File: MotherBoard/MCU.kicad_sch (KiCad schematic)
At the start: 50 parts, among them J201 Conn_ARM_SWD_TagConnect_TC2030, J202 Micro_SD_Card_Det1, U201 STM32F205RBTx, Y201 16 Mhz

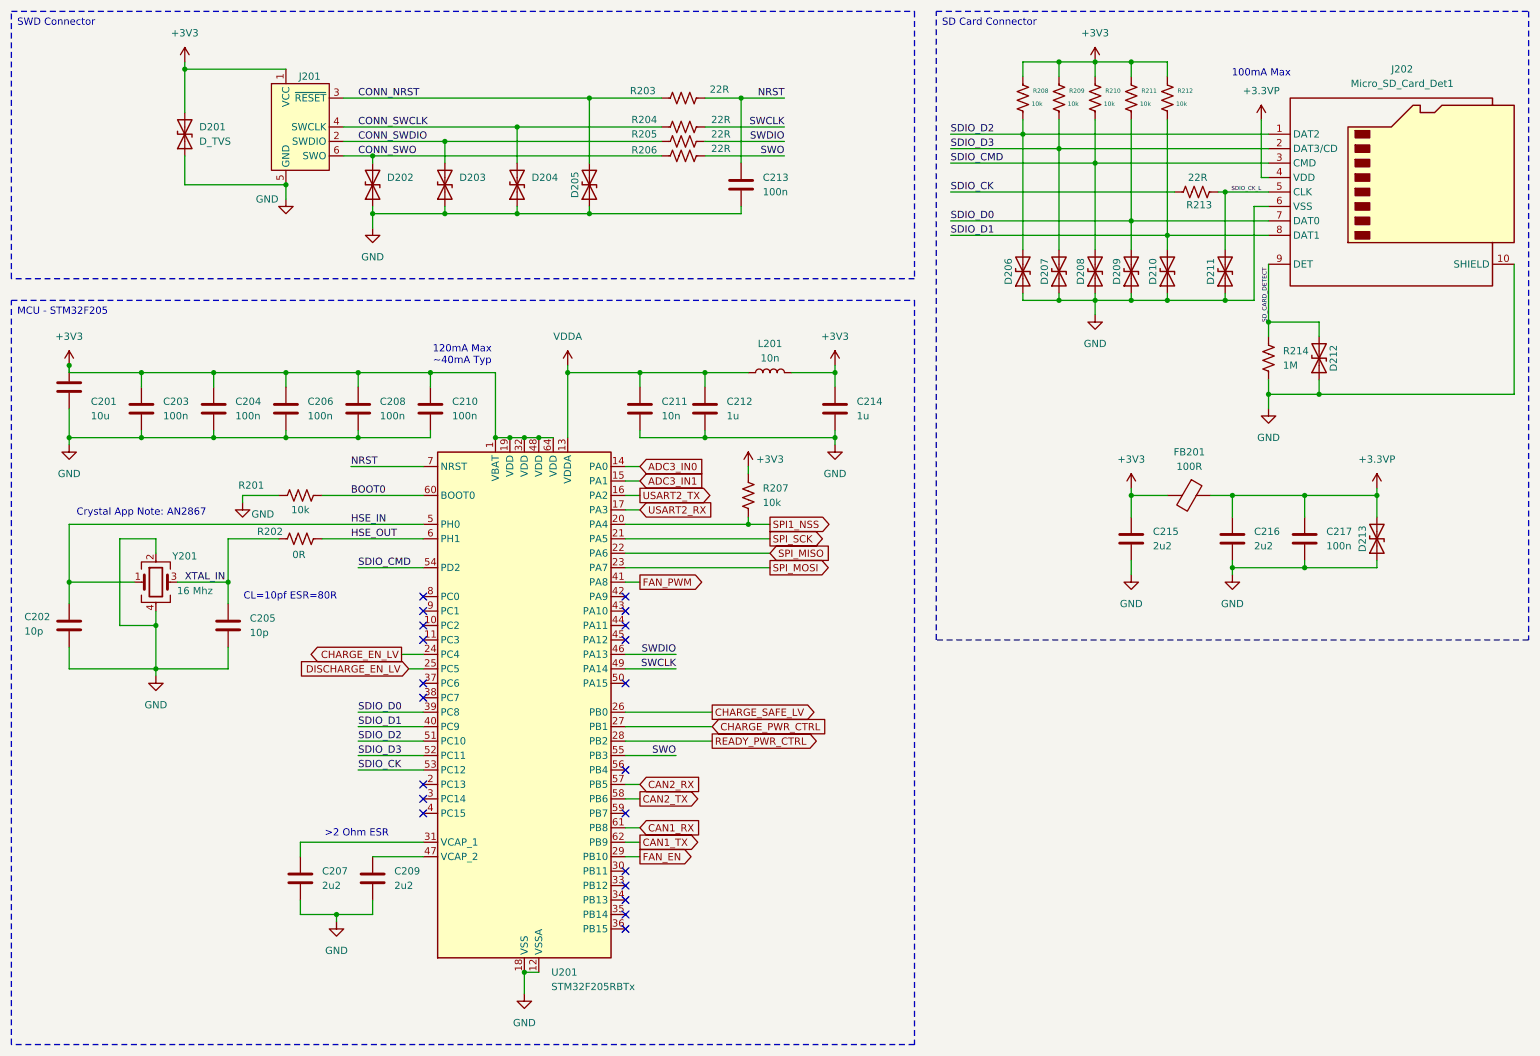
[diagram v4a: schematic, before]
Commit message: Fixed BQ79600 + minor changes
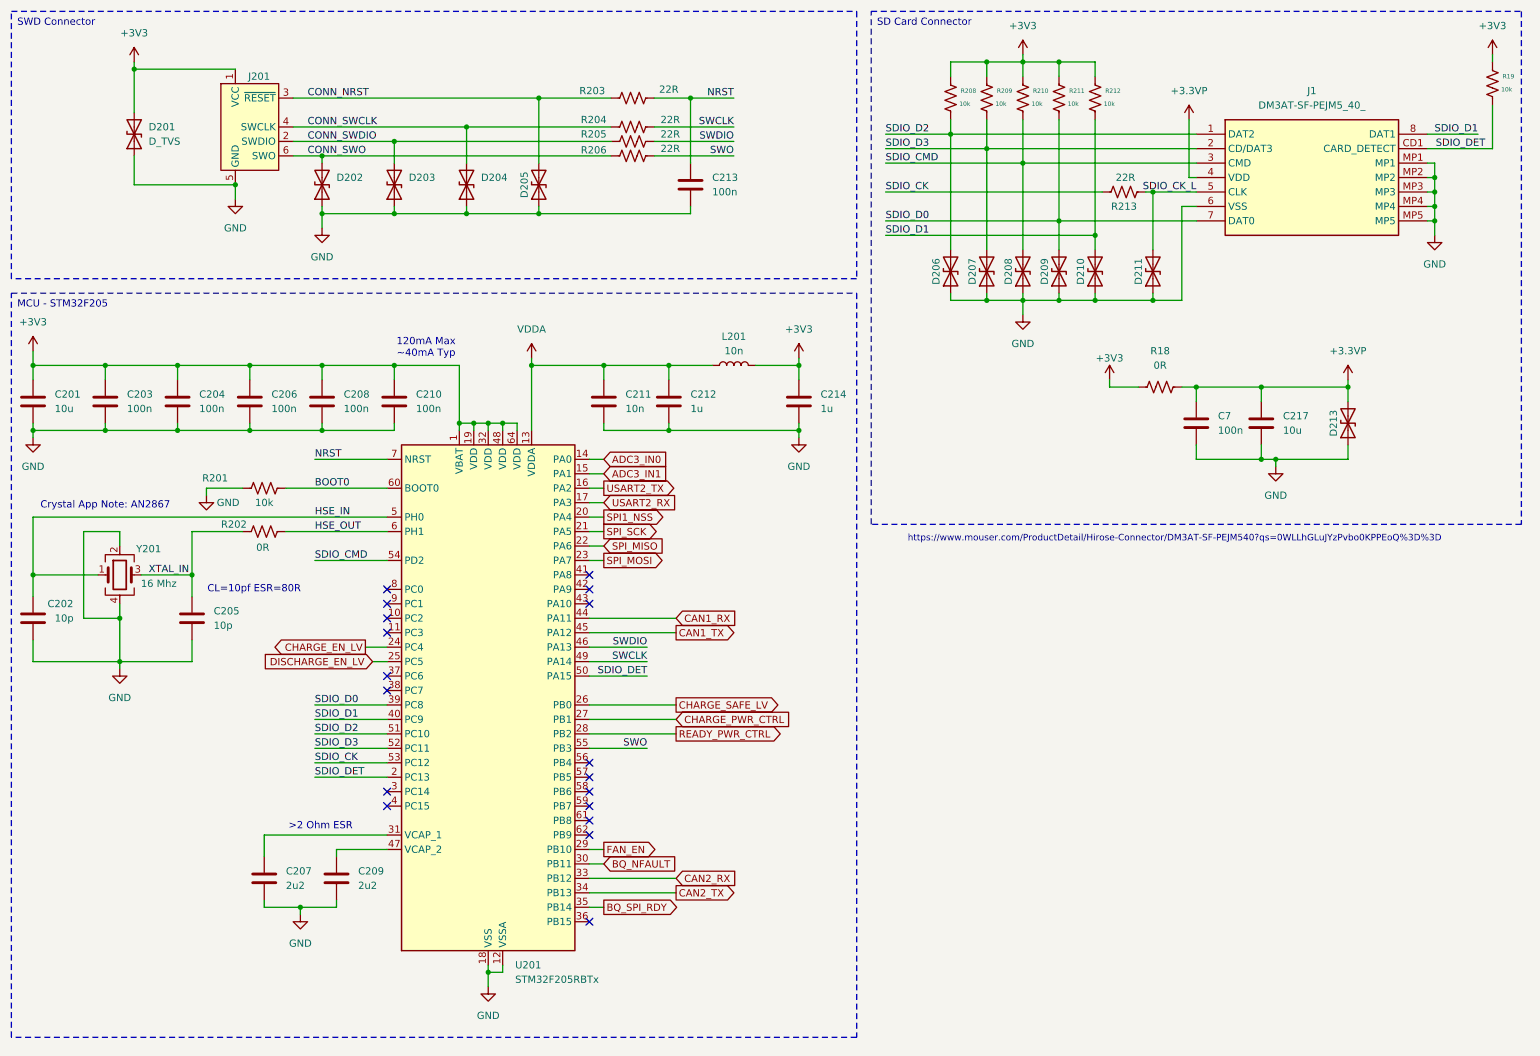
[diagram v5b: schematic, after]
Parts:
- removed C215, C216: 2u2, symbol Device:C
- removed D212: D_TVS, Diode_SMD:D_SOD-323, symbol Device:D_TVS
- removed FB201: 100R, symbol Device:FerriteBead
- removed J202: Micro_SD_Card_Det1, symbol Connector:Micro_SD_Card_Det1
- removed R207: 10k, Resistor_SMD:R_0402_1005Metric, symbol Device:R_US
- removed R214: 1M, Resistor_SMD:R_0402_1005Metric, symbol Device:R_US
- added C7: 100n, symbol Device:C
- added J1: DM3AT-SF-PEJM5_40_, SDIO:SD_CARD, symbol SDIO:DM3AT-SF-PEJM5_40_
- added R18: 0R, Resistor_SMD:R_0402_1005Metric, symbol Device:R_US
- added R19: 10k, Resistor_SMD:R_0402_1005Metric, symbol Device:R_US
- C217: value 100n -> 10u
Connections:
- net +3.3VP: now also C7.1, J1.4 (VDD), R18.2
- net +3V3: now also R18.1, R19.1
- net CAN1_RX: now also U201.44 (PA11); no longer U201.61 (PB8)
- net CAN1_TX: now also U201.45 (PA12); no longer U201.62 (PB9)
- net CAN2_RX: now also U201.33 (PB12); no longer U201.57 (PB5)
- net CAN2_TX: now also U201.34 (PB13); no longer U201.58 (PB6)
- net GND: now also C7.2, J1.6 (VSS), J1.MP1, J1.MP2, J1.MP3, J1.MP4, J1.MP5
- net SDIO_CK_L: now also J1.5 (CLK)
- net SDIO_CMD: now also J1.3 (CMD)
- net SDIO_D0: now also J1.7 (DAT0)
- net SDIO_D1: now also J1.8 (DAT1)
- net SDIO_D2: now also J1.1 (DAT2)
- net SDIO_D3: now also J1.2 (CD/DAT3)
- net SDIO_DET: now reaches U201.2 (PC13)
- net SDIO_DET: now also U201.50 (PA15), J1.CD1 (CARD_DETECT), R19.2
- net BQ_NFAULT: now reaches U201.30 (PB11)
- net BQ_SPI_RDY: now reaches U201.35 (PB14)
- net FAN_PWM: no longer names the net of U201.41 (PA8)
- no-connect marks 21 -> 18
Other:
- note added: "https://www.mouser.com/ProductDetail/Hirose-Connector/DM3AT-SF-PEJM540?qs=0WLLhGLuJYzPvbo0KPPEoQ%3D%3D"
- note removed: "100mA Max"
- moved on the sheet: C201, C202, C203, C204, C205, C206, C207, C208, C209, C210, C211, C212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

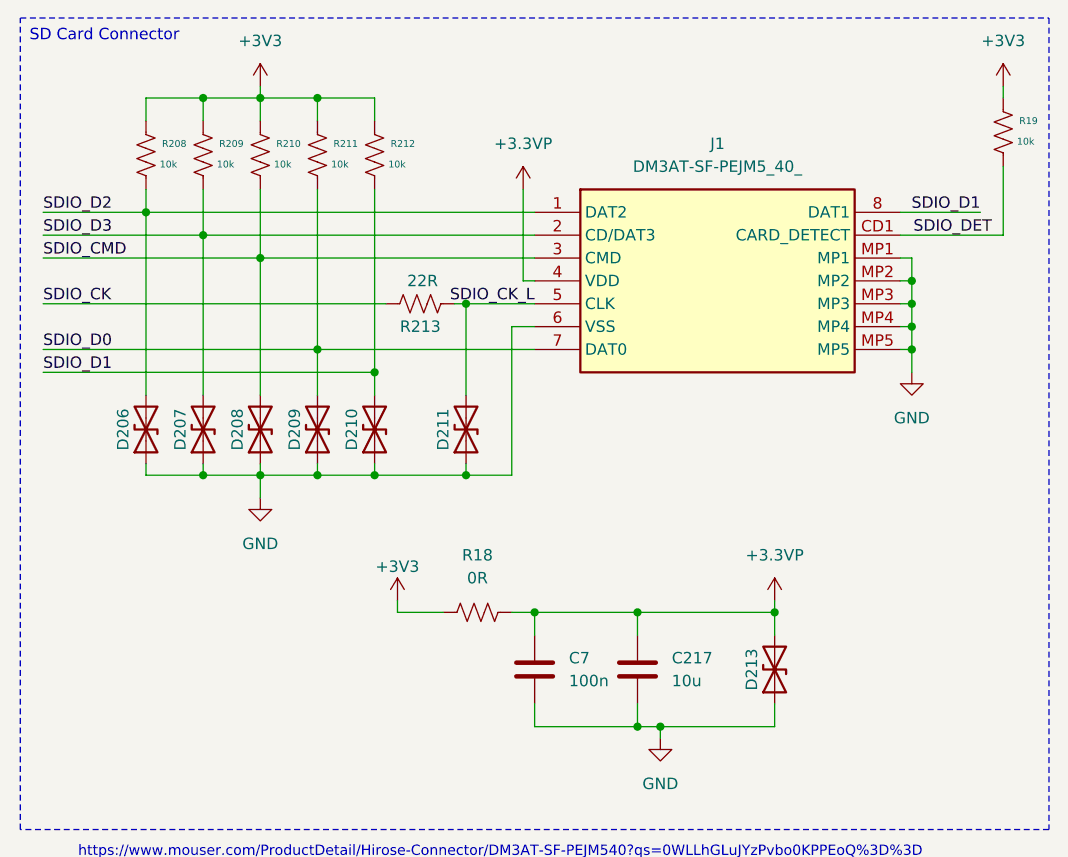
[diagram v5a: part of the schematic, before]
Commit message: Fixed CAN tranceivers + added relay driver circuit + fixed relative file paths for 3D models + finished PSU but still need correct 3D model
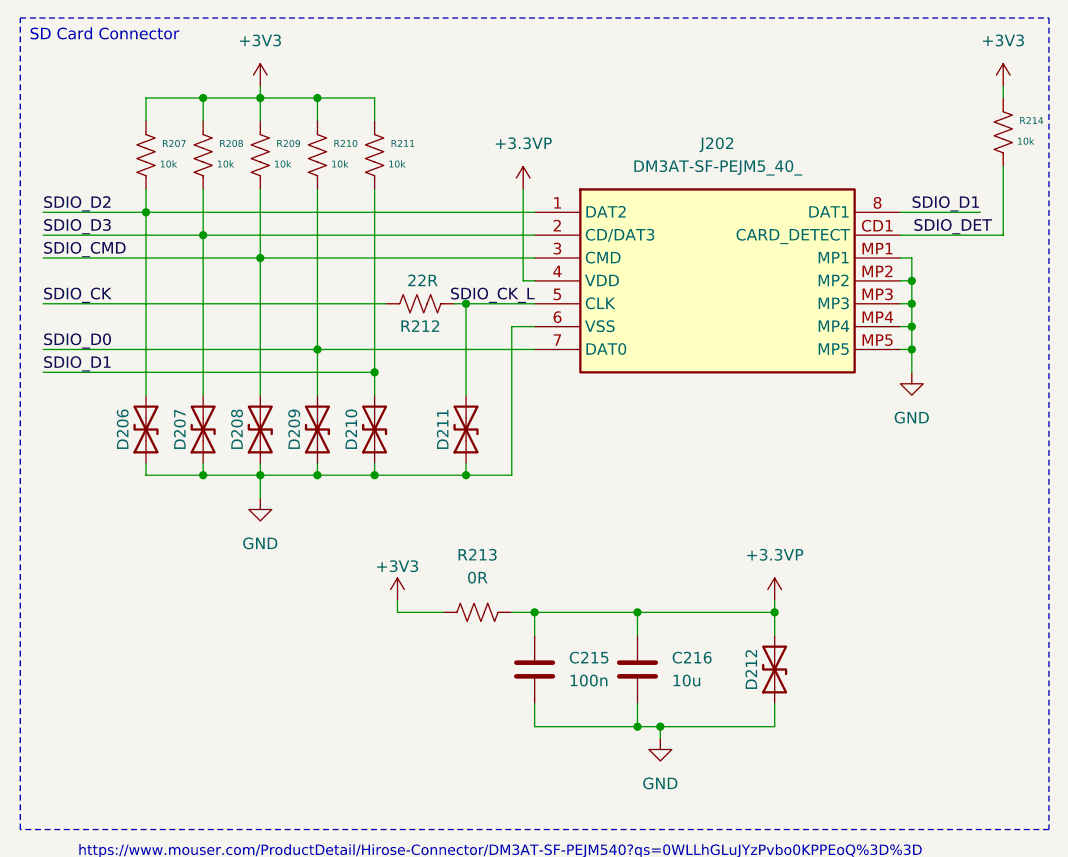
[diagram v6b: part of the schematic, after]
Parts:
- renumbered C7 to C215, C217 to C216, D213 to D212, J1 to J202, R208 to R207, R209 to R208, R210 to R209, R211 to R210, R212 to R211, R213 to R212, R18 to R213, R19 to R214
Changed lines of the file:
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@@
 		(on_board yes)
 		(dnp no)
-		(property "Reference" "#PWR0215"
+		(property "Reference" "#PWR0214"
 			(at 193.04 73.66 0)
 			(effects
@@
 			(project ""
 				(path "/335e81e9-b957-4266-8116-dde74329bfca/592735c9-cbc0-4c76-b37a-83bb0c07029e"
-					(reference "#PWR0215")
+					(reference "#PWR0214")
 					(unit 1)
 				)
@@
 		(dnp no)
 		(fields_autoplaced yes)
-		(property "Reference" "#PWR03"
+		(property "Reference" "#PWR0217"
 			(at 237.49 100.33 0)
 			(effects
@@
 			(project "FSAE_BMS"
 				(path "/335e81e9-b957-4266-8116-dde74329bfca/592735c9-cbc0-4c76-b37a-83bb0c07029e"
-					(reference "#PWR03")
+					(reference "#PWR0217")
 					(unit 1)
 				)
@@
 		(dnp no)
 		(fields_autoplaced yes)
-		(property "Reference" "R18"
+		(property "Reference" "R213"
 			(at 217.17 73.66 90)
 			(effects
@@
 			(project "FSAE_BMS"
 				(path "/335e81e9-b957-4266-8116-dde74329bfca/592735c9-cbc0-4c76-b37a-83bb0c07029e"
-					(reference "R18")
+					(reference "R213")
 					(unit 1)
 				)
@@
 		(on_board yes)
 		(dnp no)
-		(property "Reference" "R212"
+		(property "Reference" "R211"
 			(at 207.518 27.94 0)
 			(effects
@@
 			(project "FSAE_BMS"
 				(path "/335e81e9-b957-4266-8116-dde74329bfca/592735c9-cbc0-4c76-b37a-83bb0c07029e"
-					(reference "R212")
+					(reference "R211")
 					(unit 1)
 				)
@@
 		(dnp no)
 		(fields_autoplaced yes)
-		(property "Reference" "C217"
+		(property "Reference" "C216"
 			(at 238.76 85.0899 0)
 			(effects
@@
 			(project "FSAE_BMS"
 				(path "/335e81e9-b957-4266-8116-dde74329bfca/592735c9-cbc0-4c76-b37a-83bb0c07029e"
-					(reference "C217")
+					(reference "C216")
 					(unit 1)
 				)
@@
 		(dnp no)
 		(fields_autoplaced yes)
-		(property "Reference" "#PWR05"
+		(property "Reference" "#PWR0219"
 			(at 265.43 59.69 0)
 			(effects
@@
 			(project "FSAE_BMS"
 				(path "/335e81e9-b957-4266-8116-dde74329bfca/592735c9-cbc0-4c76-b37a-83bb0c07029e"
-					(reference "#PWR05")
+					(reference "#PWR0219")
 					(unit 1)
 				)
@@
 		(on_board yes)
 		(dnp no)
-		(property "Reference" "R210"
+		(property "Reference" "R209"
 			(at 194.818 27.94 0)
 			(effects
@@
 			(project "FSAE_BMS"
 				(path "/335e81e9-b957-4266-8116-dde74329bfca/592735c9-cbc0-4c76-b37a-83bb0c07029e"
-					(reference "R210")
+					(reference "R209")
 					(unit 1)
 				)
@@
 		(dnp no)
 		(fields_autoplaced yes)
-		(property "Reference" "C7"
+		(property "Reference" "C215"
 			(at 227.33 85.0899 0)
 			(effects
@@
 			(project "FSAE_BMS"
 				(path "/335e81e9-b957-4266-8116-dde74329bfca/592735c9-cbc0-4c76-b37a-83bb0c07029e"
-					(reference "C7")
+					(reference "C215")
 					(unit 1)
 				)
@@
 		(on_board yes)
 		(dnp no)
-		(property "Reference" "R209"
+		(property "Reference" "R208"
 			(at 188.468 27.94 0)
 			(effects
@@
 			(project "FSAE_BMS"
 				(path "/335e81e9-b957-4266-8116-dde74329bfca/592735c9-cbc0-4c76-b37a-83bb0c07029e"
-					(reference "R209")
+					(reference "R208")
 					(unit 1)
 				)
@@
 		(dnp no)
 		(fields_autoplaced yes)
-		(property "Reference" "#PWR0213"
+		(property "Reference" "#PWR0212"
 			(at 153.67 95.25 0)
 			(effects
@@
 			(project ""
 				(path "/335e81e9-b957-4266-8116-dde74329bfca/592735c9-cbc0-4c76-b37a-83bb0c07029e"
-					(reference "#PWR0213")
+					(reference "#PWR0212")
 					(unit 1)
 				)
@@
 		(on_board yes)
 		(dnp no)
-		(property "Reference" "R213"
+		(property "Reference" "R212"
 			(at 210.82 48.26 90)
 			(effects
@@
 			(project ""
 				(path "/335e81e9-b957-4266-8116-dde74329bfca/592735c9-cbc0-4c76-b37a-83bb0c07029e"
-					(reference "R213")
+					(reference "R212")
 					(unit 1)
 				)
@@
 		(on_board yes)
 		(dnp no)
-		(property "Reference" "R211"
+		(property "Reference" "R210"
 			(at 201.168 27.94 0)
 			(effects
@@
 			(project "FSAE_BMS"
 				(path "/335e81e9-b957-4266-8116-dde74329bfca/592735c9-cbc0-4c76-b37a-83bb0c07029e"
-					(reference "R211")
+					(reference "R210")
 					(unit 1)
 				)
@@
 		(on_board yes)
 		(dnp no)
-		(property "Reference" "R208"
+		(property "Reference" "R207"
 			(at 182.118 27.94 0)
 			(effects
@@
 			(project "FSAE_BMS"
 				(path "/335e81e9-b957-4266-8116-dde74329bfca/592735c9-cbc0-4c76-b37a-83bb0c07029e"
-					(reference "R208")
+					(reference "R207")
 					(unit 1)
 				)
@@
 		(on_board yes)
 		(dnp no)
-		(property "Reference" "#PWR0219"
+		(property "Reference" "#PWR0216"
 			(at 226.06 34.29 0)
 			(effects
@@
 			(project "FSAE_BMS"
 				(path "/335e81e9-b957-4266-8116-dde74329bfca/592735c9-cbc0-4c76-b37a-83bb0c07029e"
-					(reference "#PWR0219")
+					(reference "#PWR0216")
 					(unit 1)
 				)
@@
 		(dnp no)
 		(fields_autoplaced yes)
-		(property "Reference" "#PWR0212"
+		(property "Reference" "#PWR0211"
 			(at 153.67 78.74 0)
 			(effects
@@
 			(project "FSAE_BMS"
 				(path "/335e81e9-b957-4266-8116-dde74329bfca/592735c9-cbc0-4c76-b37a-83bb0c07029e"
-					(reference "#PWR0212")
+					(reference "#PWR0211")
 					(unit 1)
 				)
@@
 		(on_board yes)
 		(dnp no)
-		(property "Reference" "R19"
+		(property "Reference" "R214"
 			(at 277.368 25.4 0)
 			(effects
@@
 			(project "FSAE_BMS"
 				(path "/335e81e9-b957-4266-8116-dde74329bfca/592735c9-cbc0-4c76-b37a-83bb0c07029e"
-					(reference "R19")
+					(reference "R214")
 					(unit 1)
 				)
@@
 		(on_board yes)
 		(dnp no)
-		(property "Reference" "D213"
+		(property "Reference" "D212"
 			(at 247.65 86.36 0)
 			(effects
@@
 			(project "FSAE_BMS"
 				(path "/335e81e9-b957-4266-8116-dde74329bfca/592735c9-cbc0-4c76-b37a-83bb0c07029e"
-					(reference "D213")
+					(reference "D212")
 					(unit 1)
 				)
@@
 		(dnp no)
 		(fields_autoplaced yes)
-		(property "Reference" "#PWR04"
+		(property "Reference" "#PWR0220"
 			(at 275.59 25.4 0)
 			(effects
@@
 			(project "FSAE_BMS"
 				(path "/335e81e9-b957-4266-8116-dde74329bfca/592735c9-cbc0-4c76-b37a-83bb0c07029e"
-					(reference "#PWR04")
+					(reference "#PWR0220")
 					(unit 1)
 				)
@@
 		(dnp no)
 		(fields_autoplaced yes)
-		(property "Reference" "#PWR0221"
+		(property "Reference" "#PWR0218"
 			(at 254 80.01 0)
 			(effects
@@
 			(project ""
 				(path "/335e81e9-b957-4266-8116-dde74329bfca/592735c9-cbc0-4c76-b37a-83bb0c07029e"
-					(reference "#PWR0221")
+					(reference "#PWR0218")
 					(unit 1)
 				)
@@
 		(on_board yes)
 		(dnp no)
-		(property "Reference" "#PWR0216"
+		(property "Reference" "#PWR0215"
 			(at 208.28 82.55 0)
 			(effects
@@
 			(project ""
 				(path "/335e81e9-b957-4266-8116-dde74329bfca/592735c9-cbc0-4c76-b37a-83bb0c07029e"
-					(reference "#PWR0216")
+					(reference "#PWR0215")
 					(unit 1)
 				)
@@
 		(dnp no)
 		(fields_autoplaced yes)
-		(property "Reference" "#PWR0214"
+		(property "Reference" "#PWR0213"
 			(at 193.04 25.4 0)
 			(effects
@@
 			(project ""
 				(path "/335e81e9-b957-4266-8116-dde74329bfca/592735c9-cbc0-4c76-b37a-83bb0c07029e"
-					(reference "#PWR0214")
+					(reference "#PWR0213")
 					(unit 1)
 				)
@@
 		(dnp no)
 		(fields_autoplaced yes)
-		(property "Reference" "J1"
+		(property "Reference" "J202"
 			(at 243.84 27.94 0)
 			(effects
@@
 			(project ""
 				(path "/335e81e9-b957-4266-8116-dde74329bfca/592735c9-cbc0-4c76-b37a-83bb0c07029e"
-					(reference "J1")
+					(reference "J202")
 					(unit 1)
 				)
